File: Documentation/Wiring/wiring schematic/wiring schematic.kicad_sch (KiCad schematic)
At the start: 19 parts, among them K1 Relay_SPST-NO, K2 Relay_SPDT, M1 Motor_DC, M2 Motor_DC, SW1 RotaryEncoder_5pin, SW2 RotaryEncoder_5pin, SW3 SW_DPST_E-stop, SW5 SW_DPST_E-stop, SW6 SW_Push_Lamp, SW7 SW_Push_Lamp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

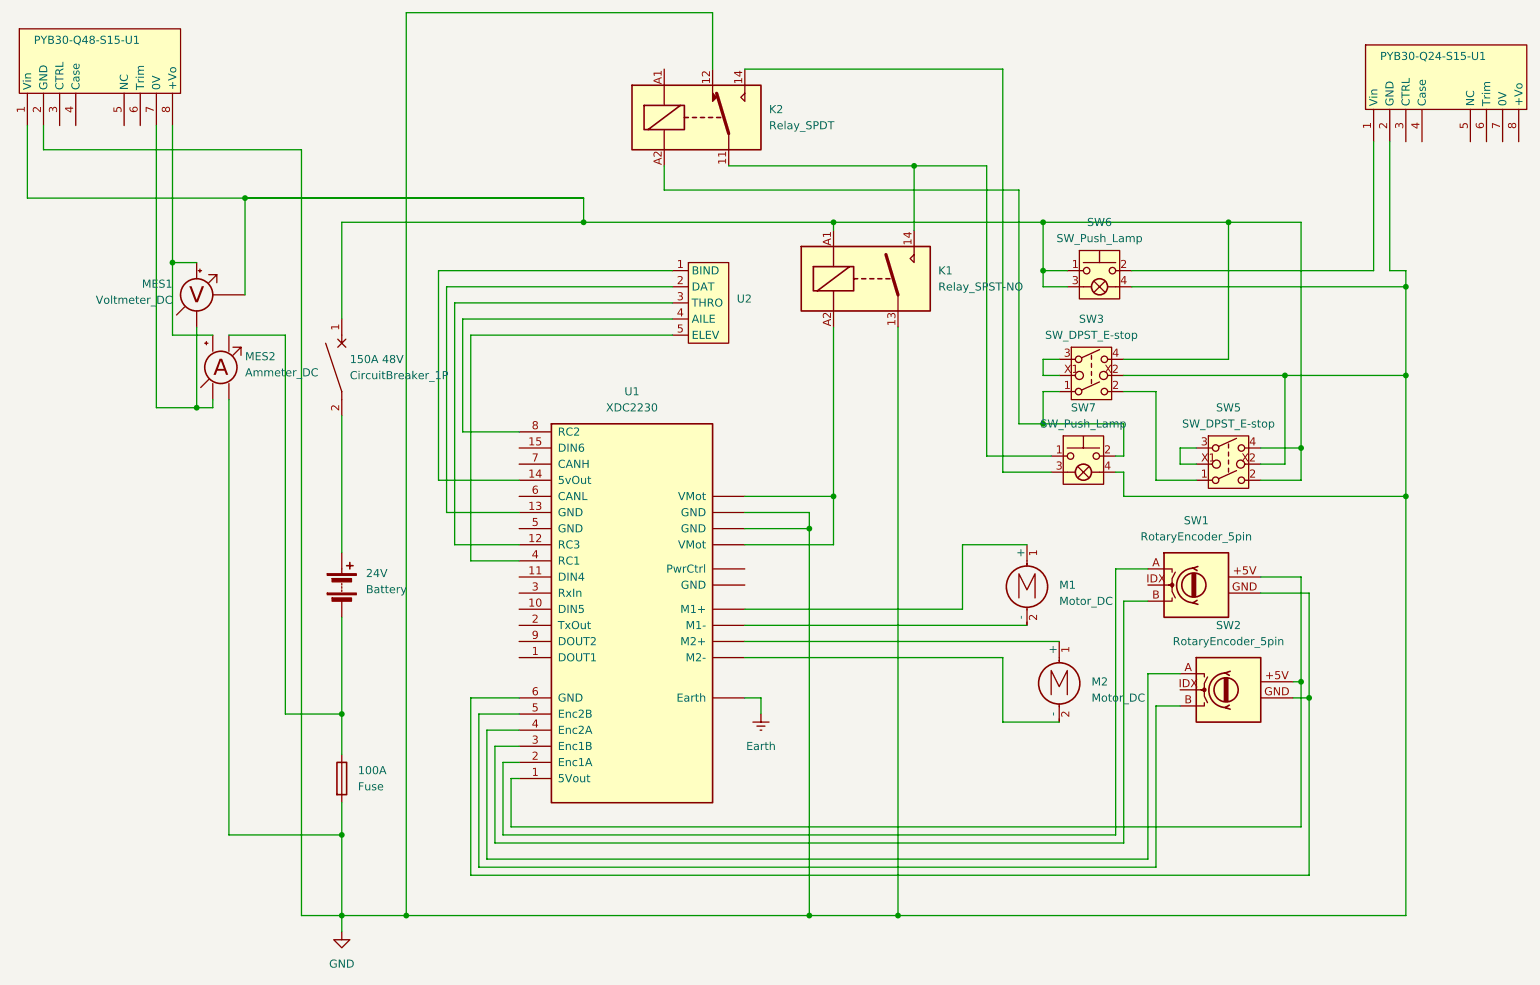
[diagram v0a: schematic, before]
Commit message: Updated kill switch to shut off 12v system
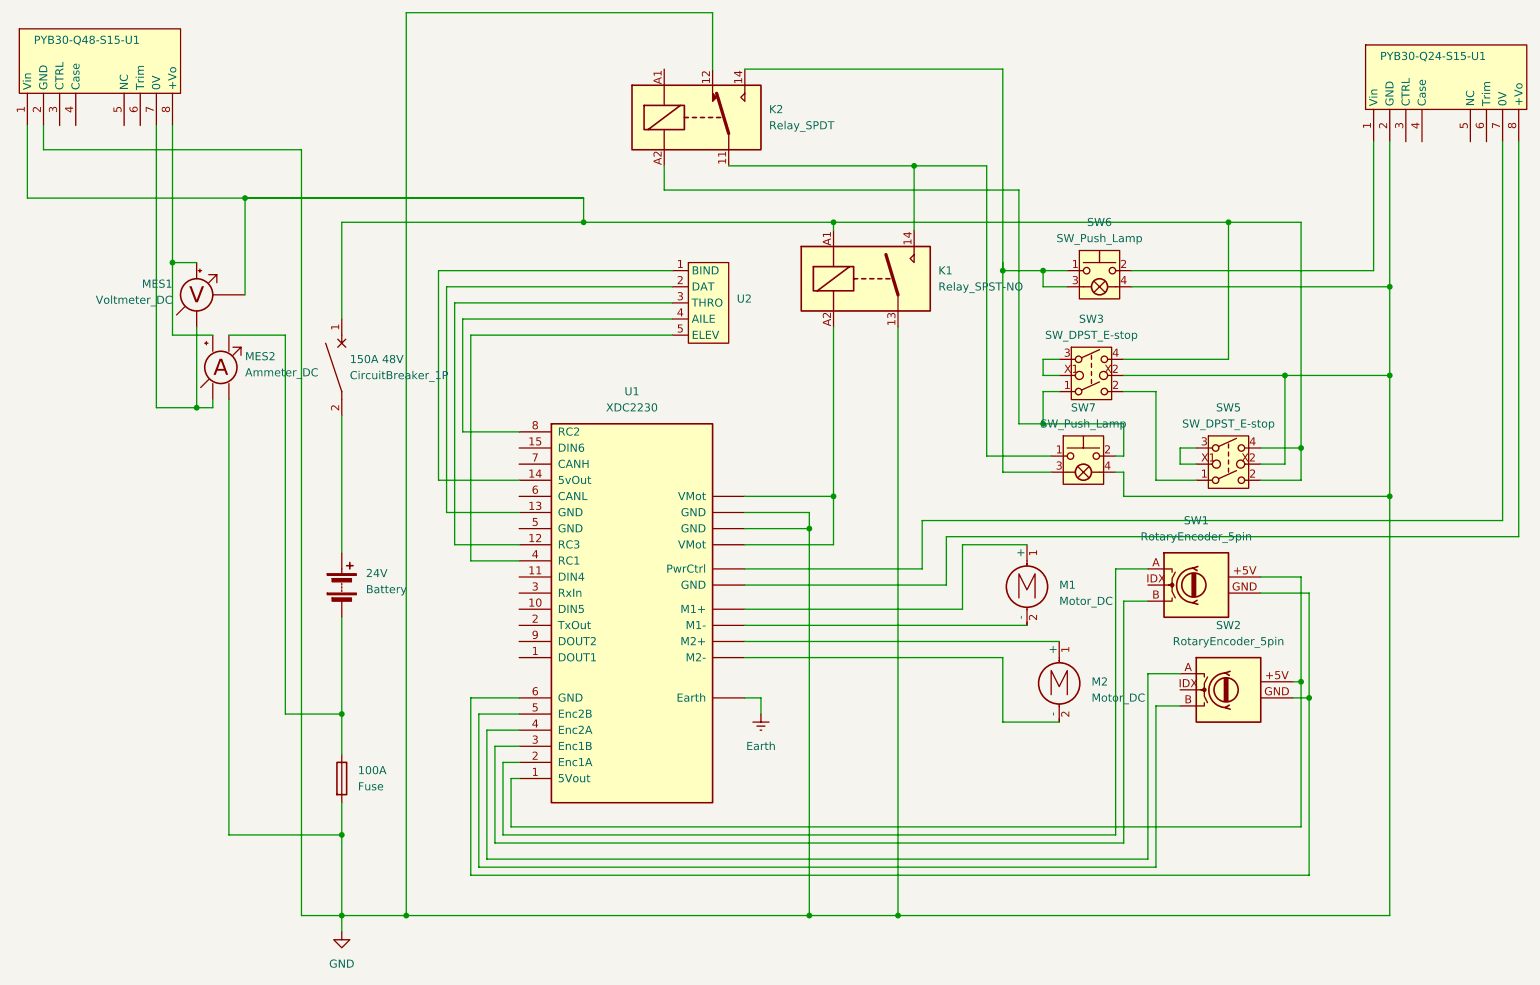
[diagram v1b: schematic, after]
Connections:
- net at K2.14, SW7.3 (L): now also SW6.1, SW6.3 (L)
- net at 150A 48V.1, K1.A1, MES1. (Vref)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: no longer SW6.1, SW6.3 (L)
- net at U1.2 (TxOut): now also SW1.A (CH_A)
- net at U1.3 (RxIn): now also SW1.B (CH_B)
- net at PYB30-Q24-S15-U1.7 (0V): now also U1. (PwrCtrl)
- net at PYB30-Q24-S15-U1.8 (+Vo): now also U1. (PwrCtrl)
